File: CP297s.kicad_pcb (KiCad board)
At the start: 2 copper layers, 155.1 x 156 mm, 111 parts, among them J1 Conn_01x05_Male, J2 Conn_01x04_Female, J3 pin header 01x15 2.54mm, J4 Conn_01x06_Female, J5 RCA-103, J6 PJ-301M, J7 PJ-301M, K1 CONN_3, K2 CONN_3, K3 TK85_BUS, P2 CONN_2, P6 CONN_2, U1 Z80, U10 74LS125, U11 74LS393, U12 74LS574, U13 74LS08, U14 74LS251, U15 74HC86, U16 74LS245, U17 74LS32, U18 74HCT00, U19 74LS138, U2 62256, U20 74HC74, U21 74HC74, U22 74LS165, U23 74LS32, U25 74LS08, U3 27256, U4 74HC04, U5 74HC74, U6 74LS393, U7 74LS11, U8 74LS32, U9 74LS245, X1 6.5MHz

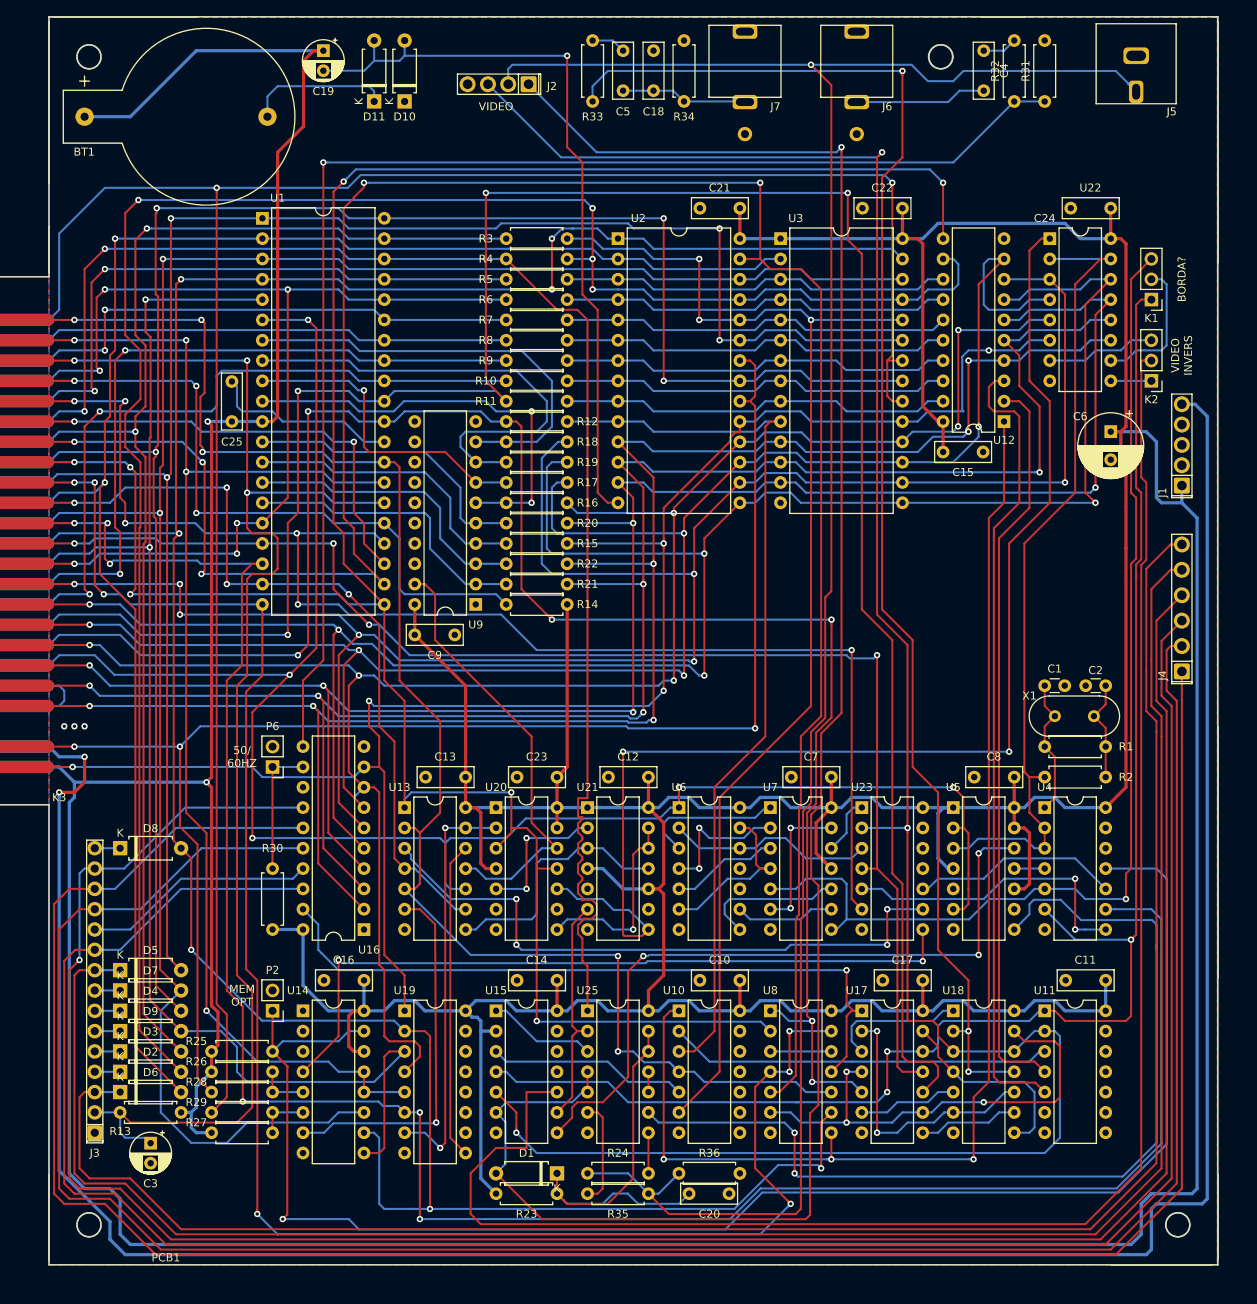
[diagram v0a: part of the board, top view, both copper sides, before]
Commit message: updated pcb layout, added logo
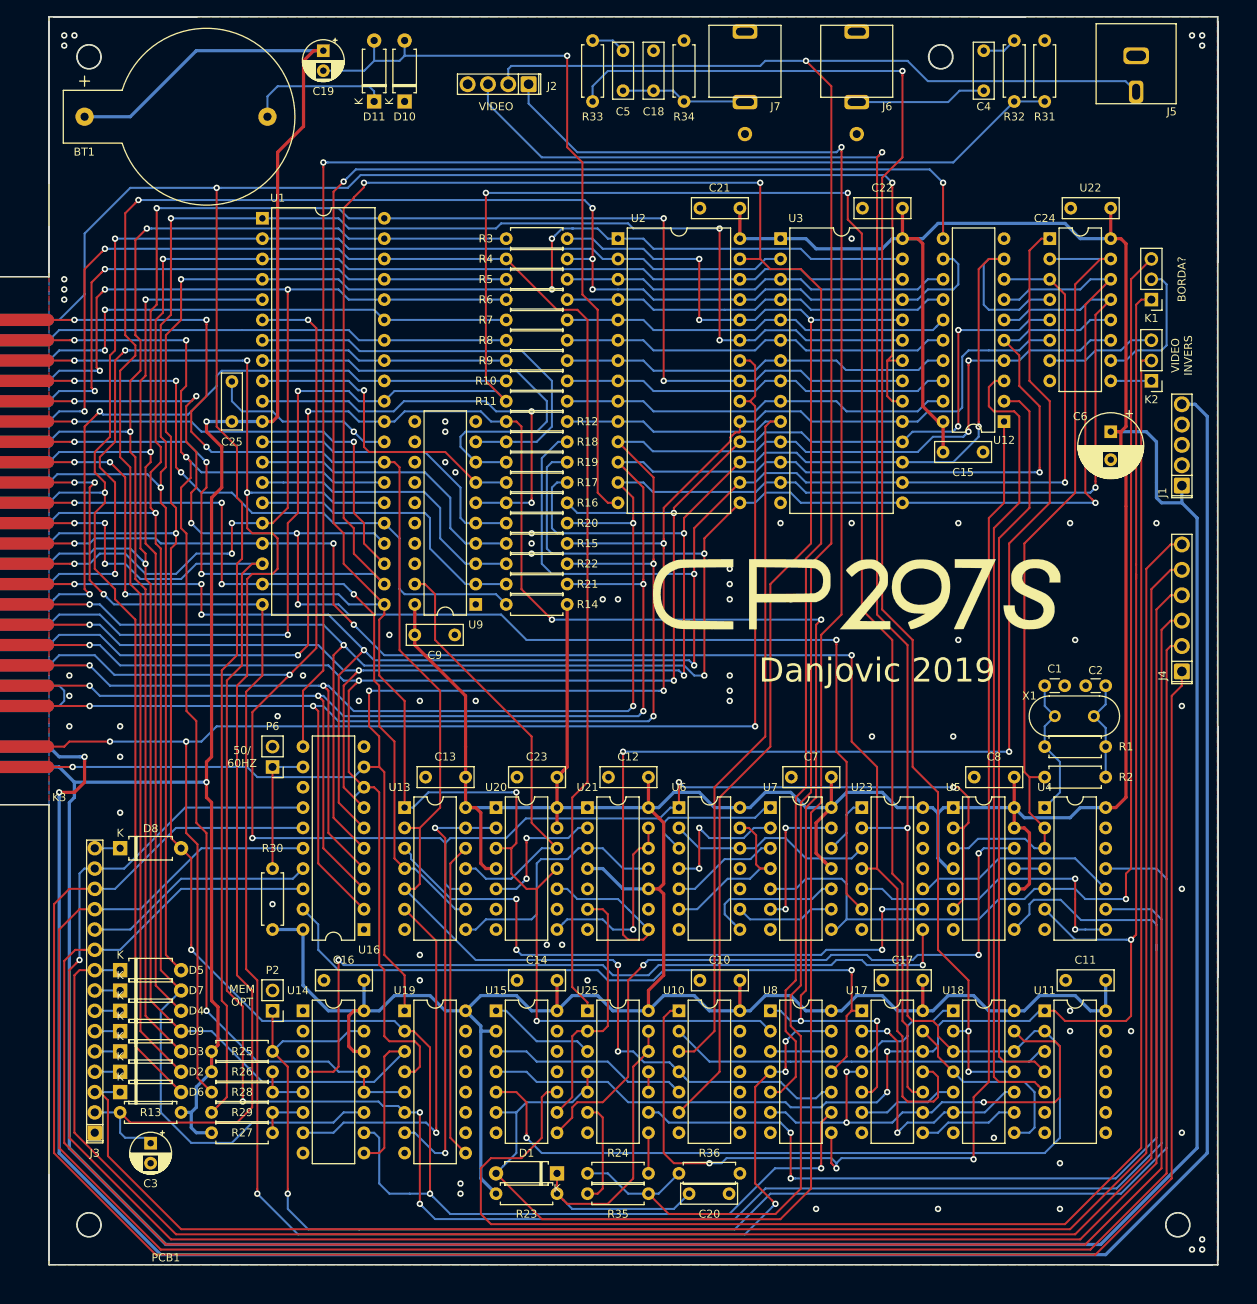
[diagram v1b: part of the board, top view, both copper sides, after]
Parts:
- added LOGO1: LOGO, CP297s:logo, F.Cu at (126.4, 119.4)
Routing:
- net ~NMI: track 171.3 -> 180.4 mm
- net +9V: track 315.8 -> 306.8 mm
- net Net-(D6-Pad1): track 236.0 -> 228.5 mm
- net Net-(J3-Pad12): track 282.7 -> 277.1 mm
- net Net-(D5-Pad1): track 250.9 -> 245.4 mm
- net A8: track 183.8 -> 178.3 mm
- net Net-(K2-Pad2): track 214.1 -> 208.8 mm
- net Net-(J3-Pad14): track 287.8 -> 283.1 mm
- net Net-(J3-Pad10): track 277.7 -> 273.0 mm
- net Net-(J3-Pad13): track 283.4 -> 279.0 mm
- net ~IORQ: track 219.3 -> 214.9 mm
- net Net-(U14-Pad4): track 93.1 -> 97.4 mm
- net A14: track 334.0 -> 329.9 mm
- net INVERT: track 28.8 -> 32.1 mm
- net Net-(U13-Pad13): track 51.9 -> 54.9 mm
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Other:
- board text added: "Danjovic 2019"

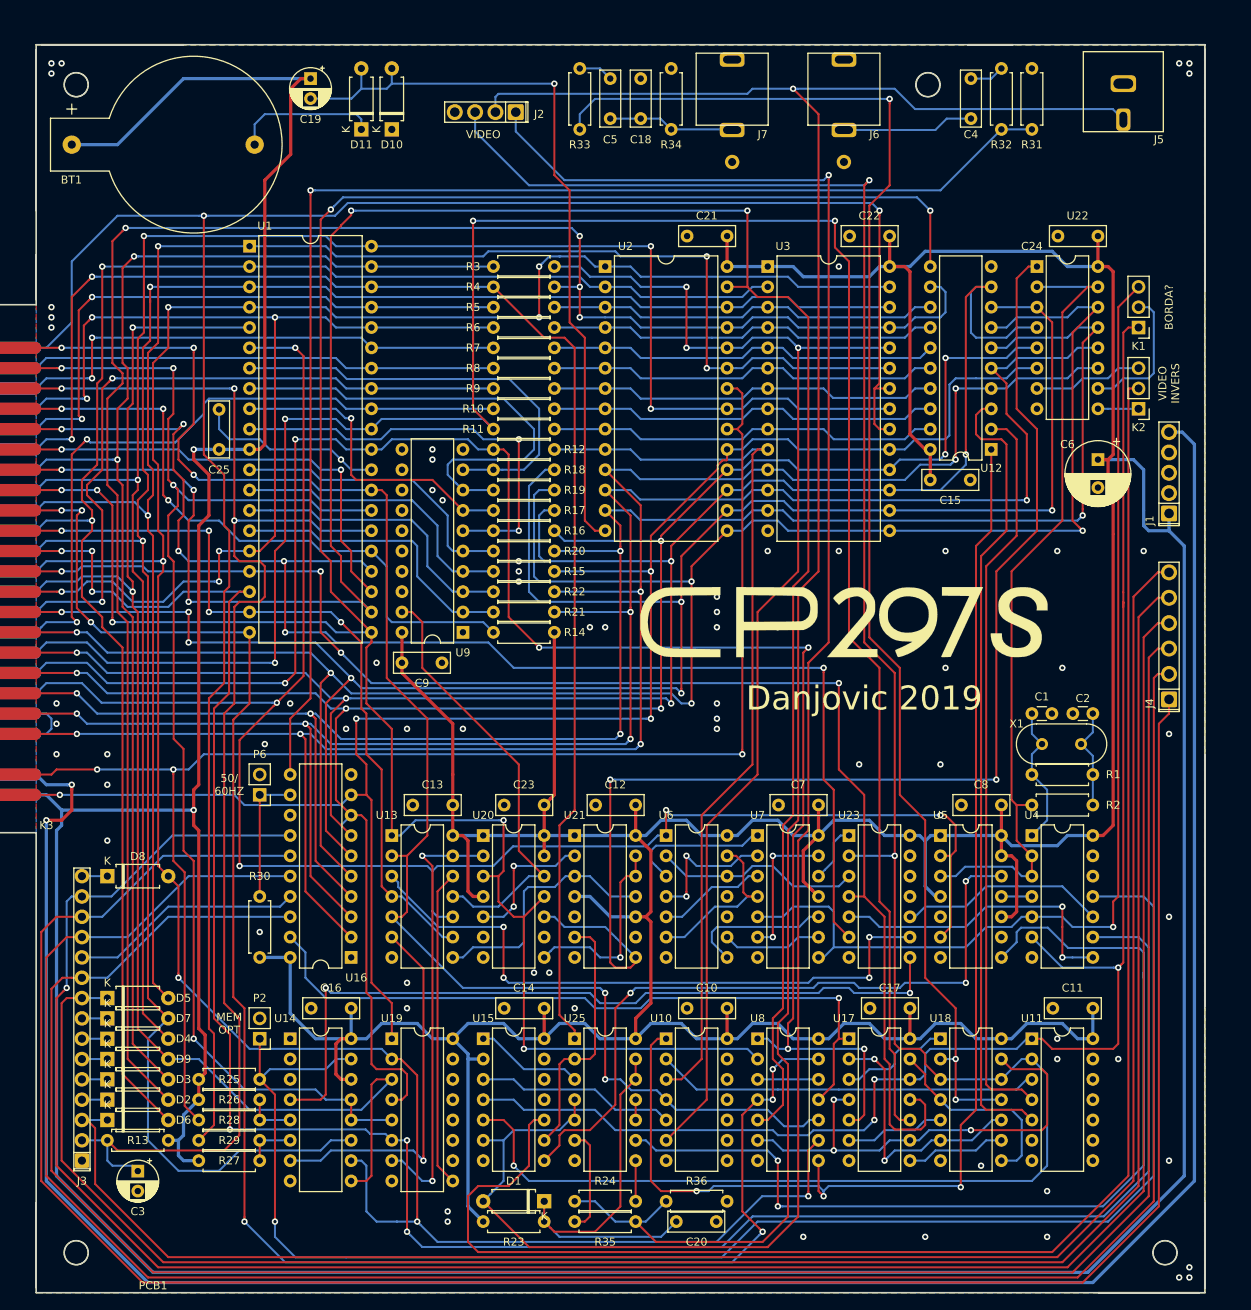
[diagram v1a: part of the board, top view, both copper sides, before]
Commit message: add PSG, changed AV connectors
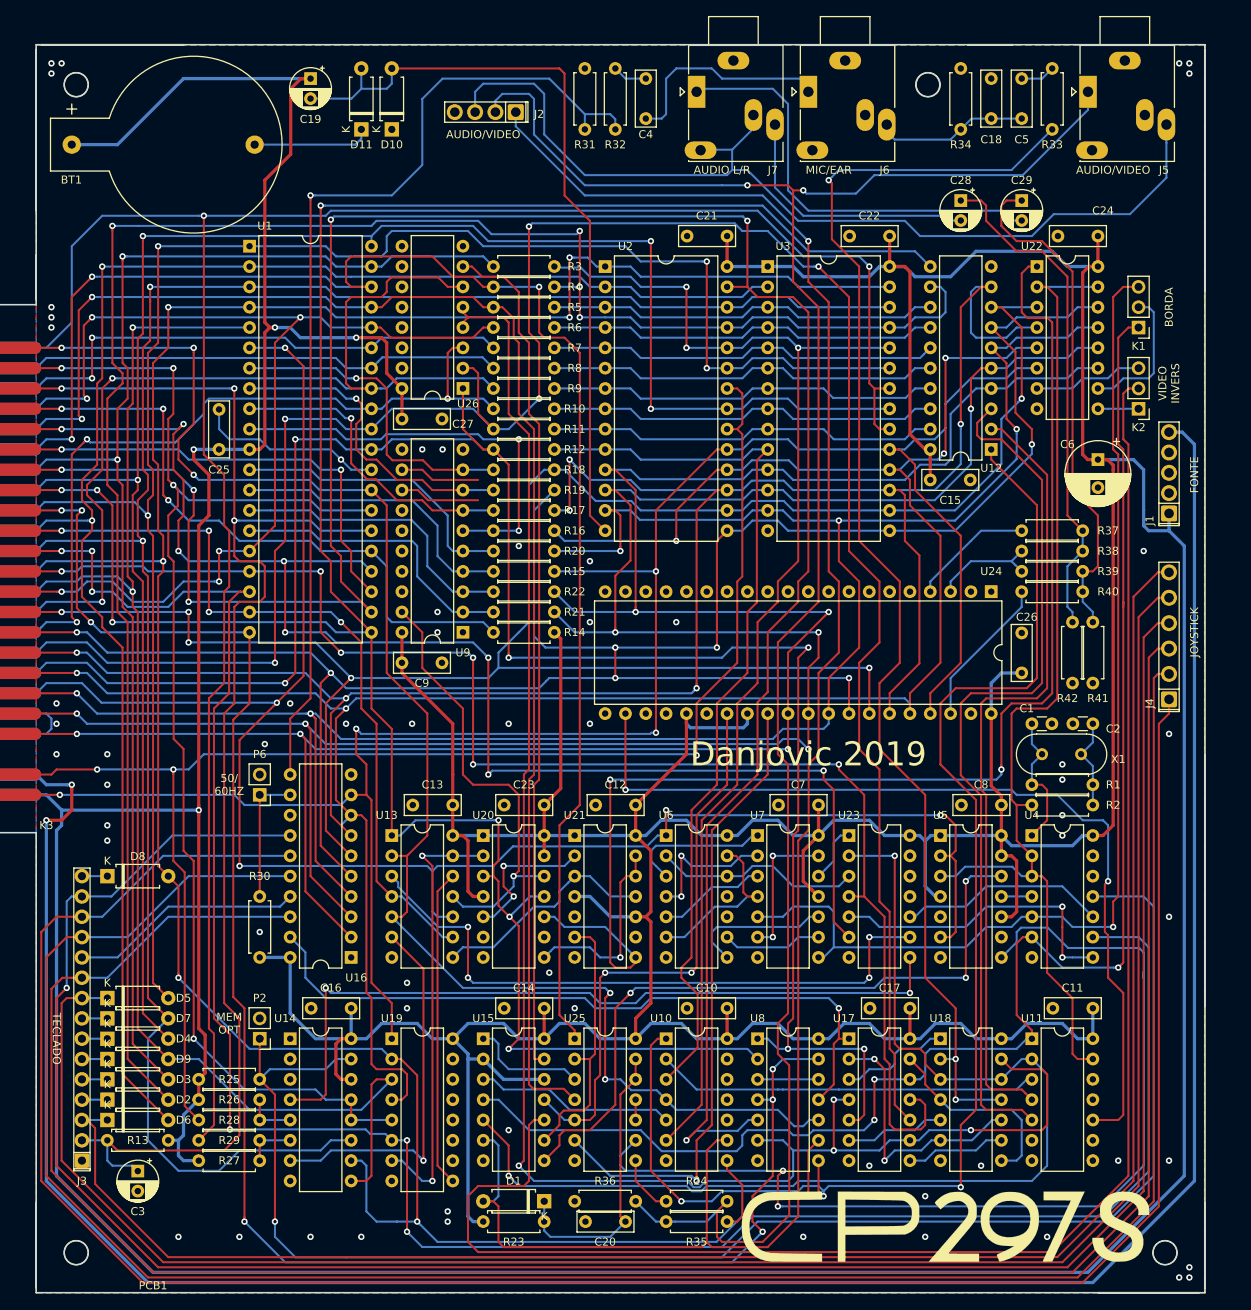
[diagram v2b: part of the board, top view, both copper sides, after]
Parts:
- added C26: 100n, Capacitor_THT:C_Disc_D7.0mm_W2.5mm_P5.00mm, F.Cu at (148.6, 125.7)
- added C27: 100n, Capacitor_THT:C_Disc_D7.0mm_W2.5mm_P5.00mm, F.Cu at (71.1, 94.0)
- added C28: 1uF, Capacitor_THT:CP_Radial_D5.0mm_P2.50mm, F.Cu at (141.0, 66.7)
- added C29: 1uF, Capacitor_THT:CP_Radial_D5.0mm_P2.50mm, F.Cu at (148.6, 66.7)
- added R37: 1k, Resistor_THT:R_Axial_DIN0207_L6.3mm_D2.5mm_P7.62mm_Horizontal, F.Cu at (148.6, 108.0)
- added R38: 2k2, Resistor_THT:R_Axial_DIN0207_L6.3mm_D2.5mm_P7.62mm_Horizontal, F.Cu at (148.6, 110.5)
- added R39: 2k2, Resistor_THT:R_Axial_DIN0207_L6.3mm_D2.5mm_P7.62mm_Horizontal, F.Cu at (148.6, 113.0)
- added R40: 1k, Resistor_THT:R_Axial_DIN0207_L6.3mm_D2.5mm_P7.62mm_Horizontal, F.Cu at (148.6, 115.6)
- added R41: 2k2, Resistor_THT:R_Axial_DIN0207_L6.3mm_D2.5mm_P7.62mm_Horizontal, F.Cu at (157.5, 119.4)
- added R42: 2k2, Resistor_THT:R_Axial_DIN0207_L6.3mm_D2.5mm_P7.62mm_Horizontal, F.Cu at (154.9, 119.4)
- added U24: AY-3-8910, Package_DIP:DIP-40_W15.24mm, F.Cu at (144.8, 115.6)
- added U26: 74LS138, Package_DIP:DIP-16_W7.62mm, F.Cu at (78.7, 90.2)
- J5: value RCA-103 -> PG203J; footprint CP297s:RCA-103 -> CP297s:PG203J
- J6, J7: value PJ-301M -> PG203J; footprint CP297s:PJ-301M -> CP297s:PG203J
- moved LOGO1 76.6 mm to (139.1, 194.9)
- moved R33 59.1 mm to (152.4, 57.8)
- moved R31 55.9 mm to (94.0, 57.8)
- moved C5 51.4 mm to (148.6, 51.4)
- moved R32 48.3 mm to (97.8, 57.8)
- moved C18 43.8 mm to (144.8, 51.4)
- moved C4 40.6 mm to (101.6, 51.4)
- moved R34 36.2 mm to (141.0, 57.8)
- moved R24 19.1 mm to (111.8, 191.8), turned to 180 degrees
- moved R35 19.1 mm to (111.8, 194.3), turned to 180 degrees
- moved R36 19.1 mm to (92.7, 191.8), turned to 0 degrees
- moved J6 6.56 mm to (121.9, 53.1), turned to 270 degrees
- moved J7 6.56 mm to (108.0, 53.1), turned to 270 degrees
- moved C20 6.35 mm to (99.1, 194.3), turned to 180 degrees
- moved J5 4.53 mm to (156.9, 53.1), turned to 270 degrees
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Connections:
- net Net-(U17-Pad4) renamed ~IOWR
- J2 pad 3: VSYNC -> AUDIO-MONO
- J5 pad 2: GND -> AUDIO-MONO
- J6 pad 1: GND -> /EAR
- J6 pad 2: /EAR -> /MIC
- J6 pad 3: Net-(J6-Pad3) -> GND
- J7 pad 1: GND -> /AUDIO-R
- J7 pad 2: /MIC -> /AUDIO-L
- J7 pad 3: Net-(J7-Pad3) -> GND
- U10 pad 10: (no net) -> GND
- U10 pad 8: (no net) -> Net-(R35-Pad1)
- U10 pad 9: (no net) -> ~CSYNC
- U11 pad 10: (no net) -> /1.625MHz
- U11 pad 11: (no net) -> Net-(U11-Pad11)
- U11 pad 12: (no net) -> GND
- U11 pad 13: (no net) -> 6.5M
- U11 pad 8: (no net) -> Net-(U11-Pad8)
- U11 pad 9: (no net) -> Net-(U11-Pad9)
- U15 pad 11: (no net) -> Net-(U15-Pad11)
- U15 pad 12: (no net) -> +5V
- U15 pad 13: (no net) -> Net-(U15-Pad13)
- U25 pad 4: ~CSYNC -> A7
- U25 pad 5: ~CSYNC -> Net-(U15-Pad11)
- U25 pad 6: Net-(R35-Pad1) -> Net-(U24-Pad29)
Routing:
- net ~IOWR: track 59.1 -> 213.7 mm, vias 3 -> 4
- net VSYNC: track 282.2 -> 141.8 mm, vias 3 -> 2
- net AUDIO-MONO: track 0.00 -> 122.4 mm
- net /1.625MHz: track 0.00 -> 113.1 mm, vias 0 -> 2
- net A7: track 73.0 -> 180.8 mm
- net Net-(U15-Pad13): track 0.00 -> 106.8 mm
- net +5V: track 1083.8 -> 1167.1 mm, vias 2 -> 4
- net Net-(U24-Pad29): track 0.00 -> 79.4 mm, vias 0 -> 1
- net Net-(U15-Pad11): track 0.00 -> 71.6 mm, vias 0 -> 2
- net Net-(C29-Pad1): track 0.00 -> 63.8 mm
- net Net-(C28-Pad1): track 0.00 -> 63.4 mm
- net /AUDIO-R: track 0.00 -> 53.9 mm
- net D6': track 238.5 -> 287.9 mm, vias 6 -> 5
- net D0': track 225.0 -> 269.1 mm, vias 6 -> 5
- net D1': track 230.9 -> 271.9 mm, vias 5 -> 6
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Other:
- board text added: "AUDIO L/R"
- board text added: "AUDIO/VIDEO"
- board text added: "BORDA"
- board text added: "FONTE"
- board text added: "JOYSTICK"
- board text added: "MIC/EAR"
- board text added: "TECLADO"
- board text removed: "BORDA?"
- board text removed: "VIDEO"
